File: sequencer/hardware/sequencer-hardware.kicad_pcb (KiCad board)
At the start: 4 copper layers, 100.6 x 151.4 mm, 125 parts, among them J1 Barrel Jack, J10 JST_4-pin_male, J11 Conn_01x03, J12 Conn_01x03, J13 Conn_01x03, J14 Conn_01x03, J15 JST_4-pin_male, J16 JST_4-pin_male, J17 Conn_01x03, J2 40Pin 0.1"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

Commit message: Add star ground point
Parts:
- added JP1: SolderJumper_2_Bridged, custom:SolderJumper-2_P1.3mm_Bridged_Pad1.0x1.5mm, F.Cu at (34.7, 60.5)
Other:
- board text added: "D.R.U.M. Sequencer HW Design REV: 1.0 Layout REV: A Order No. P/N DRUM-SQ-1000"
- board text added: "STAR GND"
- board text removed: "D.R.U.M. - Module HW Design REV: 1.0 Layout REV: A Order No. P/N DRUM-DM-1001"
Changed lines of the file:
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@@
     )
   )
+  (footprint "custom:SolderJumper-2_P1.3mm_Bridged_Pad1.0x1.5mm" (layer "F.Cu")
+    (at 34.671 60.452 -90)
+    (descr "SMD Solder Jumper, 1x1.5mm Pads, 0.3mm gap, bridged with 1 copper strip")
+    (tags "net tie solder jumper bridged")
+    (property "Sheetfile" "File: sequencer-hardware.kicad_sch")
+    (property "Sheetname" "")
+    (attr exclude_from_pos_files)
+    (fp_text reference "JP1" (at -3.429 0) (layer "F.SilkS")
+      (effects (font (size 1 1) (thickness 0.15)))
+    )
+    (fp_text value "SolderJumper_2_Bridged" (at 0 1.9 90) (layer "F.Fab")
+      (effects (font (size 1 1) (thickness 0.15)))
+    )
+    (fp_poly (pts
+        (xy -0.3008 -1.2096)
+        (xy 0.3008 -1.2096)
+        (xy 0.3008 -0.6096)
+        (xy -0.3008 -0.6096)
+      ) (layer "F.Cu") (width 0) (fill solid))
+    (fp_poly (pts
+        (xy -0.3048 -0.2952)
+        (xy 0.2968 -0.2952)
+        (xy 0.2968 0.3048)
+        (xy -0.3048 0.3048)
+      ) (layer "F.Cu") (width 0) (fill solid))
+    (fp_poly (pts
+        (xy -0.3048 0.6192)
+        (xy 0.2968 0.6192)
+        (xy 0.2968 1.2192)
+        (xy -0.3048 1.2192)
+      ) (layer "F.Cu") (width 0) (fill solid))
+    (fp_line (start -2.54 1.905) (end -2.54 -1.905) (layer "F.SilkS") (width 0.12))
+    (fp_line (start -2.54 -1.905) (end 2.54 -1.905) (layer "F.SilkS") (width 0.12))
+    (fp_line (start 2.54 -1.905) (end 2.54 1.905) (layer "F.SilkS") (width 0.12))
+    (fp_line (start 2.54 1.905) (end -2.54 1.905) (layer "F.SilkS") (width 0.12))
+    (fp_line (start -2.54 -1.905) (end 2.54 -1.905) (layer "F.CrtYd") (width 0.05))
+    (fp_line (start -2.54 -1.905) (end -2.54 1.905) (layer "F.CrtYd") (width 0.05))
+    (fp_line (start 2.54 1.905) (end 2.54 -1.905) (layer "F.CrtYd") (width 0.05))
+    (fp_line (start 2.54 1.905) (end -2.54 1.905) (layer "F.CrtYd") (width 0.05))
+    (pad "1" smd rect (at -1.27 0 270) (size 2 3) (layers "F.Cu" "F.Mask")
+      (net 2 "GNDA") (pinfunction "A") (pintype "passive"))
+    (pad "2" smd rect (at 1.27 0 270) (size 2 3) (layers "F.Cu" "F.Mask")
+      (net 72 "GNDD") (pinfunction "B") (pintype "passive"))
+  )
   (footprint "Resistor_SMD:R_0603_1608Metric_Pad0.98x0.95mm_HandSolder" (layer "F.Cu")
     (at 38.824 141.313 180)
@@
   (gr_line (start 82.55 87.63) (end 81.915 88.9) (layer "F.SilkS") (width 0.15))
   (gr_line (start 105.41 77.47) (end 106.68 76.2) (layer "F.SilkS") (width 0.15))
-  (gr_line (start 32.766 60.452) (end 26.162 60.452) (layer "F.SilkS") (width 0.15))
+  (gr_line (start 32.7152 60.452) (end 26.162 60.452) (layer "F.SilkS") (width 0.15))
   (gr_line (start 74.93 88.9) (end 88.9 88.9) (layer "F.SilkS") (width 0.15))
   (gr_line (start 101.092 78.486) (end 98.552 75.946) (layer "F.SilkS") (width 0.15))
@@
   (gr_line (start 78.74 86.36) (end 77.47 87.63) (layer "F.SilkS") (width 0.15))
   (gr_line (start 97.155 110.49) (end 100.965 110.49) (layer "F.SilkS") (width 0.15))
-  (gr_line (start 75.438 60.452) (end 36.576 60.452) (layer "F.SilkS") (width 0.15))
+  (gr_line (start 75.438 60.452) (end 36.6268 60.452) (layer "F.SilkS") (width 0.15))
   (gr_line (start 104.14 90.17) (end 102.87 90.17) (layer "F.SilkS") (width 0.15))
   (gr_line (start 99.06 106.68) (end 100.33 105.41) (layer "F.SilkS") (width 0.15))
@@
       (xy 25.4 176.784)
     ) (layer "Edge.Cuts") (width 0.1) (fill none))
-  (gr_text "D.R.U.M. - Module\nHW Design REV: 1.0\nLayout REV: A\nOrder No.    \nP/N DRUM-DM-1001" (at 52.07 166.37) (layer "B.SilkS")
+  (gr_text "D.R.U.M.\nSequencer\nHW Design REV: 1.0\nLayout REV: A\nOrder No.    \nP/N DRUM-SQ-1000" (at 52.07 166.37) (layer "B.SilkS")
     (effects (font (size 1 1) (thickness 0.2)) (justify mirror))
   )
@@
     (effects (font (size 1 1) (thickness 0.150084)) (justify right))
   )
+  (gr_text "STAR\n\nGND" (at 32.385 60.452) (layer "F.SilkS")
+    (effects (font (size 1 1) (thickness 0.2)) (justify right))
+  )
   (gr_text "2022 D.R.U.M. Design Team\nZach Baldwin\nAndy Regli\nMark Vaughn" (at 52.07 166.37) (layer "F.SilkS")
     (effects (font (size 1 1) (thickness 0.2)))
@@
   (segment (start 40.063 157.03) (end 41.148 158.115) (width 0.2) (layer "F.Cu") (net 3))
   (segment (start 85.682 128.694) (end 86.3375 128.694) (width 0.2) (layer "F.Cu") (net 3))
-  (segment (start 83.207 128.6045) (end 83.207 128.3125) (width 0.2) (layer "F.Cu") (net 3))
   (segment (start 80.899 124.8145) (end 82.0155 124.8145) (width 0.508) (layer "F.Cu") (net 3))
   (segment (start 87.3495 126.9735) (end 87.376 127) (width 0.2) (layer "F.Cu") (net 3))
@@
   (segment (start 91.694 73.025) (end 88.2415 69.5725) (width 0.508) (layer "F.Cu") (net 71))
   (segment (start 80.607 134.2772) (end 80.6196 134.2898) (width 0.2) (layer "F.Cu") (net 72))
-  (segment (start 80.607 132.042) (end 78.3718 132.042) (width 0.2) (layer "F.Cu") (net 72))
   (segment (start 80.607 129.8066) (end 80.6196 129.794) (width 0.2) (layer "F.Cu") (net 72))
-  (segment (start 78.4352 132.0292) (end 78.359 132.0292) (width 0.2) (layer "F.Cu") (net 72))
   (segment (start 92.4315 101.234) (end 92.059 101.6065) (width 0.508) (layer "F.Cu") (net 72))
   (segment (start 79.607 135.4795) (end 79.607 133.042) (width 0.2) (layer "F.Cu") (net 72))
@@
   (segment (start 95.123 101.234) (end 92.4315 101.234) (width 0.508) (layer "F.Cu") (net 72))
   (segment (start 80.607 132.042) (end 82.842 132.042) (width 0.2) (layer "F.Cu") (net 72))
+  (segment (start 78.397 132.042) (end 78.359 132.08) (width 0.2) (layer "F.Cu") (net 72))
   (segment (start 101.6715 101.219) (end 102.059 101.6065) (width 0.508) (layer "F.Cu") (net 72))
-  (segment (start 78.3718 132.042) (end 78.359 132.0292) (width 0.2) (layer "F.Cu") (net 72))
   (segment (start 48 77.0625) (end 47.5 76.5625) (width 0.508) (layer "F.Cu") (net 72))
   (segment (start 79.607 133.042) (end 80.607 132.042) (width 0.2) (layer "F.Cu") (net 72))
@@
   (segment (start 69.939 120.104) (end 69.977 120.142) (width 0.508) (layer "F.Cu") (net 72))
   (segment (start 80.607 132.042) (end 80.607 134.2772) (width 0.2) (layer "F.Cu") (net 72))
-  (segment (start 78.486 132.08) (end 78.4352 132.0292) (width 0.2) (layer "F.Cu") (net 72))
   (segment (start 74.2895 110.1145) (end 74.295 110.109) (width 0.508) (layer "F.Cu") (net 72))
+  (segment (start 80.607 132.042) (end 78.397 132.042) (width 0.2) (layer "F.Cu") (net 72))
   (via (at 103.632 82.931) (size 0.8) (drill 0.4) (layers "F.Cu" "B.Cu") (free) (net 72))
   (via (at 87.757 89.916) (size 0.8) (drill 0.4) (layers "F.Cu" "B.Cu") (free) (net 72))
@@
   (via (at 53.721 77.343) (size 0.8) (drill 0.4) (layers "F.Cu" "B.Cu") (free) (net 72))
   (via (at 69.977 120.142) (size 0.8) (drill 0.4) (layers "F.Cu" "B.Cu") (net 72))
-  (via (at 78.359 132.0292) (size 0.8) (drill 0.4) (layers "F.Cu" "B.Cu") (net 72))
+  (via (at 78.359 132.08) (size 0.8) (drill 0.4) (layers "F.Cu" "B.Cu") (net 72))
   (via (at 57.277 76.2) (size 0.8) (drill 0.4) (layers "F.Cu" "B.Cu") (free) (net 72))
   (via (at 68.961 72.517) (size 0.8) (drill 0.4) (layers "F.Cu" "B.Cu") (free) (net 72))
@@
     (polygon
       (pts
-        (xy 49.784 168.656)
-        (xy 46.99 168.656)
-        (xy 46.99 167.259)
-        (xy 49.784 167.259)
+        (xy 49.784 169.418)
+        (xy 46.99 169.418)
+        (xy 46.99 168.021)
+        (xy 49.784 168.021)
       )
     )

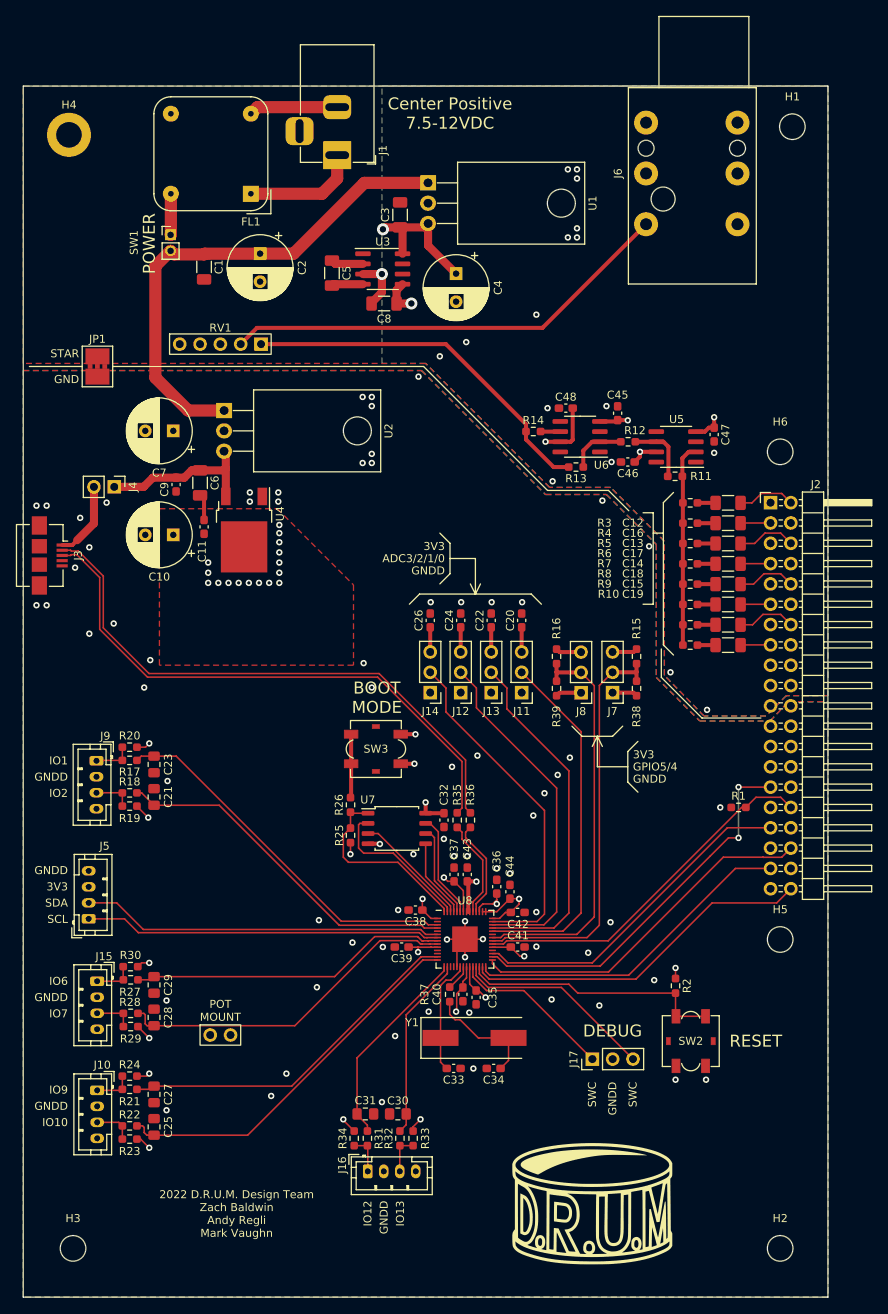
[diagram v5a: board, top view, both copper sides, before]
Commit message: Add testpoints
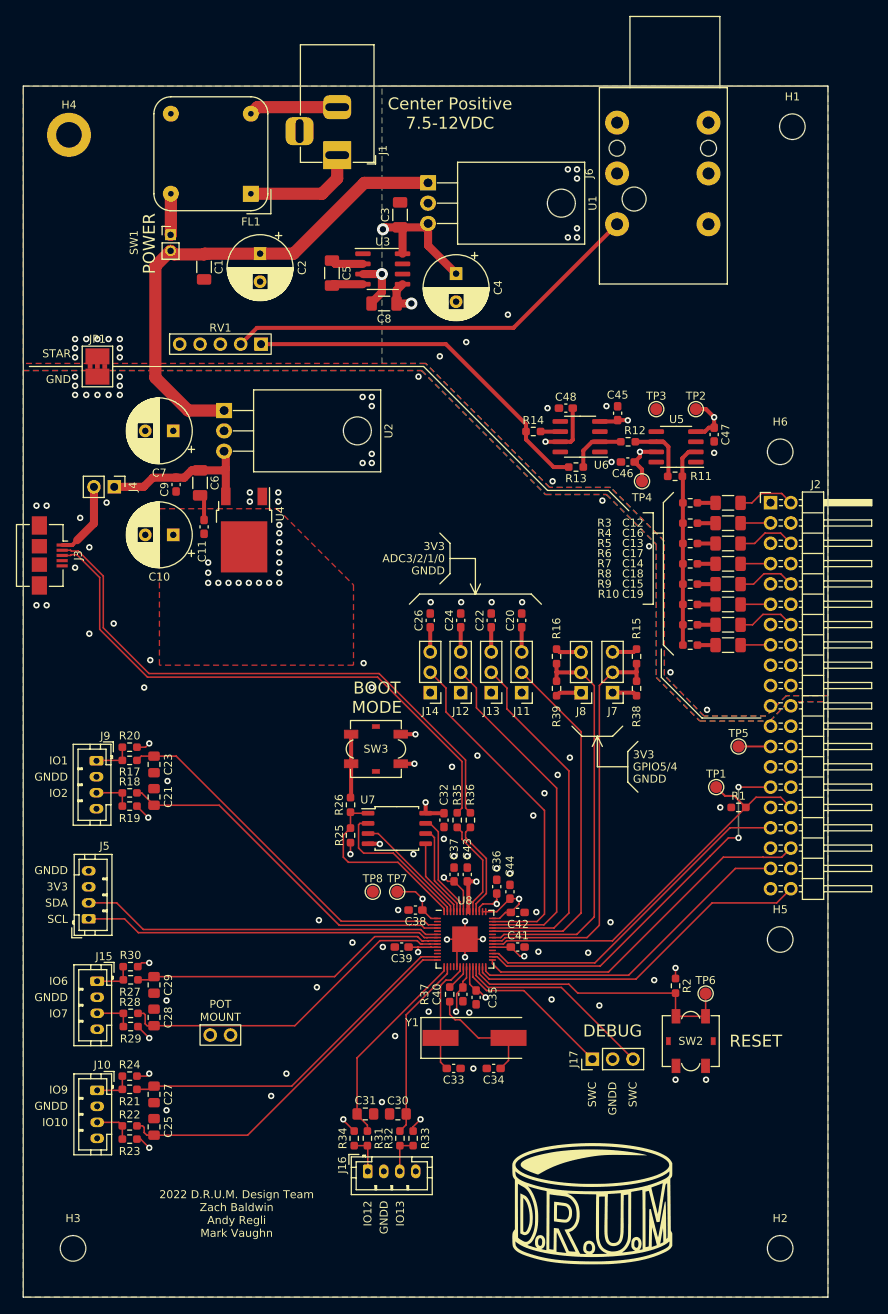
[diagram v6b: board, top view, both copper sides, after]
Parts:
- added TP1: TestPoint, TestPoint:TestPoint_Pad_D1.5mm, F.Cu at (112.0, 113.0)
- added TP2: TestPoint, TestPoint:TestPoint_Pad_D1.5mm, F.Cu at (109.5, 65.8)
- added TP3: TestPoint, TestPoint:TestPoint_Pad_D1.5mm, F.Cu at (104.5, 65.8)
- added TP4: TestPoint, TestPoint:TestPoint_Pad_D1.5mm, F.Cu at (102.7, 74.8)
- added TP5: TestPoint, TestPoint:TestPoint_Pad_D1.5mm, F.Cu at (114.8, 108.0)
- added TP6: TestPoint, TestPoint:TestPoint_Pad_D1.5mm, F.Cu at (110.7, 138.8)
- added TP7: TestPoint, TestPoint:TestPoint_Pad_D1.5mm, F.Cu at (72.1, 126.1)
- added TP8: TestPoint, TestPoint:TestPoint_Pad_D1.5mm, F.Cu at (69.1, 126.1)
- moved J6 3.62 mm to (99.6, 42.7)
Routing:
- net /CBUS_NEXTPRSNT: track 45.4 -> 50.2 mm
- net +5VD: track 20.6 -> 24.7 mm
- net Net-(J6-PadT): track 56.9 -> 53.3 mm
- net +3V3: track 73.7 -> 77.2 mm
- net /RUN: track 33.0 -> 35.9 mm
- net -5V: track 53.2 -> 56.0 mm
- net +5VA: track 24.4 -> 27.1 mm
- net GNDD: vias 75 -> 84
- net GNDA: vias 17 -> 26

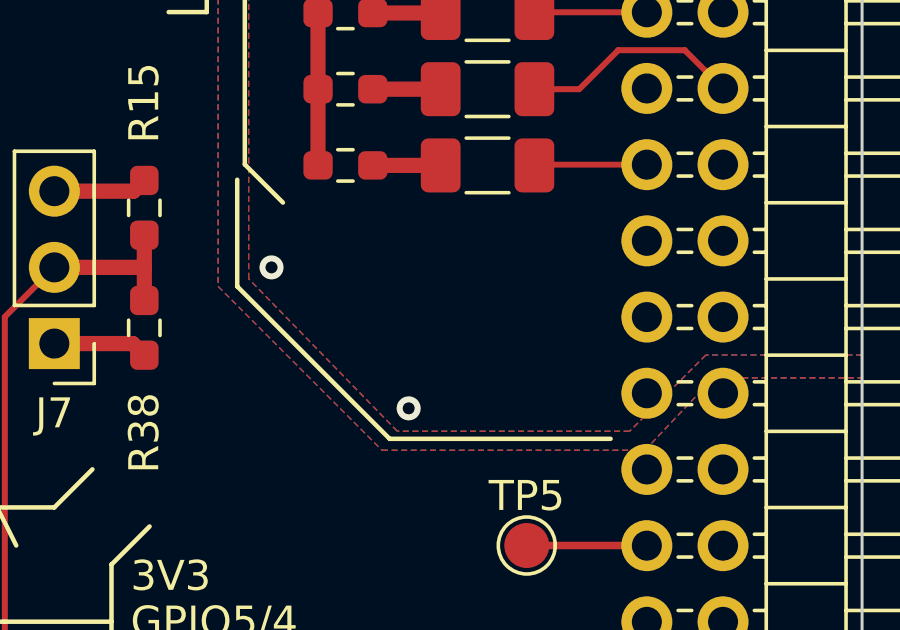
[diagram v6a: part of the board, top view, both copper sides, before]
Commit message: Add final mounting hole and generate STEP file
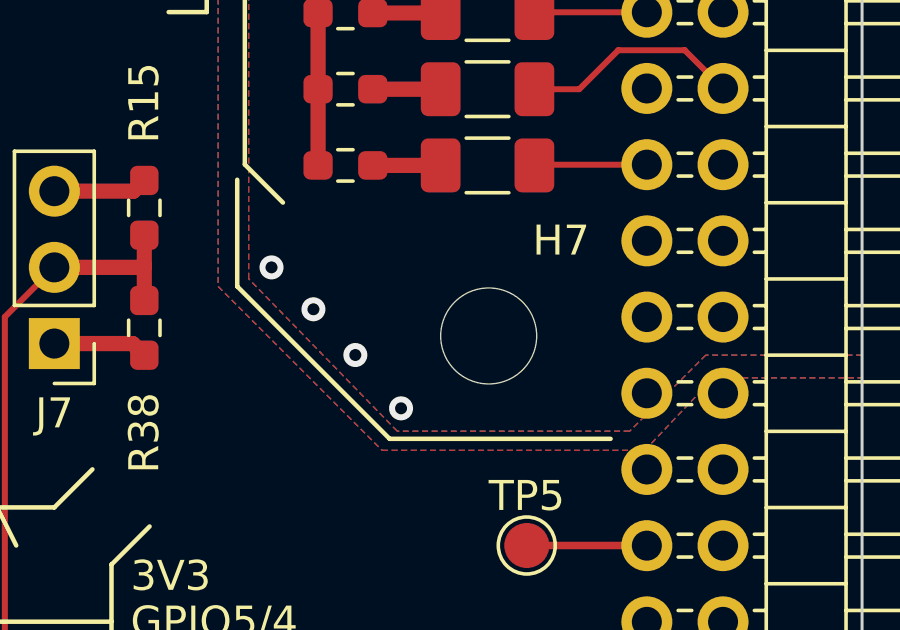
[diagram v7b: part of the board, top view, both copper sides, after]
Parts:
- added H7: MountingHole, MountingHole:MountingHole_3.2mm_M3_ISO14580, F.Cu at (113.5, 101.0)
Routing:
- net GNDA: vias 26 -> 28
